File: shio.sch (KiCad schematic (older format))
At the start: 85 parts, among them J1 USB_B_Micro, U1 LM66100DCKT, U2 MAX38640AENT+, U3 NRF52840-CKAA-R7, U4 LM66100DCKT, U5 BMA400, U6 W25N01GVZEIG_TR, Y1 32.768kHz, Y2 32MHz

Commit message: All footprints are ok in layout
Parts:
- removed BAT1: 1.8V-3.6V, Shio:CR1632-THRU, symbol Device:Battery_Cell
- removed J1: USB_B_Micro, digikey-footprints:USB_Micro_B_Female_10118193-0001LF, symbol Connector:USB_B_Micro
- added J?: 10118193-0001LF, digikey-footprints:USB_Micro_B_Female_10118193-0001LF, symbol dk_USB-DVI-HDMI-Connectors:10118193-0001LF
- added U7: CR1632, Shio:CR1632-THRU, symbol CR1632:CR1632
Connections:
- wire segments 204 -> 205
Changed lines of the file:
@@
 FLASH_SCLK
-$Comp
-L Device:Battery_Cell BAT1
-U 1 1 5EF31146
-P 9650 2900
-F 0 "BAT1" H 9768 2996 50  0000 L CNN
-F 1 "1.8V-3.6V" H 9768 2905 50  0000 L CNN
-F 2 "Shio:CR1632-THRU" V 9650 2960 50  0001 C CNN
-F 3 "~" V 9650 2960 50  0001 C CNN
-	1    9650 2900
-	1    0    0    -1
-$EndComp
 $Comp
 L power:GND #PWR018
@@
 $EndComp
 $Comp
-L Connector:USB_B_Micro J1
-U 1 1 5ED1C5A9
-P 10450 2800
-F 0 "J1" H 10507 3267 50  0000 C CNN
-F 1 "USB_B_Micro" H 10507 3176 50  0000 C CNN
-F 2 "digikey-footprints:USB_Micro_B_Female_10118193-0001LF" H 10600 2750 50  0001 C CNN
-F 3 "~" H 10600 2750 50  0001 C CNN
-	1    10450 2800
-	1    0    0    -1
-$EndComp
-$Comp
 L power:GND #PWR019
 U 1 1 5ED1D7D8
-P 10450 3200
-F 0 "#PWR019" H 10450 2950 50  0001 C CNN
-F 1 "GND" H 10455 3027 50  0000 C CNN
-F 2 "" H 10450 3200 50  0001 C CNN
-F 3 "" H 10450 3200 50  0001 C CNN
-	1    10450 3200
-	1    0    0    -1
-$EndComp
-Wire Wire Line
-	10350 3200 10450 3200
-Connection ~ 10450 3200
-Wire Wire Line
-	10800 2800 10750 2800
-Wire Wire Line
-	10800 2900 10750 2900
-Text Label 10800 2800 0    50   ~ 0
+P 10900 2400
+F 0 "#PWR019" H 10900 2150 50  0001 C CNN
+F 1 "GND" H 10905 2227 50  0000 C CNN
+F 2 "" H 10900 2400 50  0001 C CNN
+F 3 "" H 10900 2400 50  0001 C CNN
+	1    10900 2400
+	1    0    0    -1
+$EndComp
+Wire Wire Line
+	10800 2400 10900 2400
+Wire Wire Line
+	10850 2100 10800 2100
+Wire Wire Line
+	10850 2200 10800 2200
+Text Label 10850 2100 0    50   ~ 0
 SWDCLK
-Text Label 10800 2900 0    50   ~ 0
+Text Label 10850 2200 0    50   ~ 0
 SWDIO
 Text Label 10650 5450 2    50   ~ 0
@@
 Connection ~ 1500 6950
 Connection ~ 1500 7250
-Wire Wire Line
-	9650 3000 9650 3050
 $Comp
 L Device:R_Small_US R10
@@
 	0    1    1    0
 $EndComp
-NoConn ~ 10750 3000
+NoConn ~ 10800 2300
 Wire Wire Line
 	8100 2950 8350 2950
-Wire Wire Line
-	9650 2700 9650 2550
 Text Label 7550 2950 0    50   ~ 0
 VDD_nRF
@@
 L power:VBUS #PWR09
 U 1 1 5F9001CA
-P 10850 2500
-F 0 "#PWR09" H 10850 2350 50  0001 C CNN
-F 1 "VBUS" H 10865 2673 50  0000 C CNN
-F 2 "" H 10850 2500 50  0001 C CNN
-F 3 "" H 10850 2500 50  0001 C CNN
-	1    10850 2500
-	1    0    0    -1
-$EndComp
-Wire Wire Line
-	10850 2500 10850 2600
-Wire Wire Line
-	10750 2600 10850 2600
+P 10900 1900
+F 0 "#PWR09" H 10900 1750 50  0001 C CNN
+F 1 "VBUS" H 10915 2073 50  0000 C CNN
+F 2 "" H 10900 1900 50  0001 C CNN
+F 3 "" H 10900 1900 50  0001 C CNN
+	1    10900 1900
+	1    0    0    -1
+$EndComp
+Wire Wire Line
+	10900 1900 10900 2000
+Wire Wire Line
+	10800 2000 10900 2000
 $Comp
 L power:+BATT #PWR010
@@
 Wire Wire Line
 	7900 1700 7950 1700
+$Comp
+L CR1632:CR1632 U7
+U 1 1 5FA2470C
+P 9750 2750
+F 0 "U7" H 9888 2719 50  0000 L CNN
+F 1 "CR1632" H 9888 2628 50  0000 L CNN
+F 2 "Shio:CR1632-THRU" H 9750 2750 50  0001 C CNN
+F 3 "" H 9750 2750 50  0001 C CNN
+	1    9750 2750
+	1    0    0    -1
+$EndComp
+Wire Wire Line
+	9650 2550 9650 2750
+Wire Wire Line
+	9650 2950 9650 3050
+$Comp
+L dk_USB-DVI-HDMI-Connectors:10118193-0001LF J?
+U 1 1 5FA5986B
+P 10500 2200
+F 0 "J?" H 10564 2945 60  0000 C CNN
+F 1 "10118193-0001LF" H 10564 2839 60  0000 C CNN
+F 2 "digikey-footprints:USB_Micro_B_Female_10118193-0001LF" H 10700 2400 60  0001 L CNN
+F 3 "http://www.amphenol-icc.com/media/wysiwyg/files/drawing/10118193.pdf" H 10700 2500 60  0001 L CNN
+F 4 "609-4616-1-ND" H 10700 2600 60  0001 L CNN "Digi-Key_PN"
+F 5 "10118193-0001LF" H 10700 2700 60  0001 L CNN "MPN"
+F 6 "Connectors, Interconnects" H 10700 2800 60  0001 L CNN "Category"
+F 7 "USB, DVI, HDMI Connectors" H 10700 2900 60  0001 L CNN "Family"
+F 8 "http://www.amphenol-icc.com/media/wysiwyg/files/drawing/10118193.pdf" H 10700 3000 60  0001 L CNN "DK_Datasheet_Link"
+F 9 "/product-detail/en/amphenol-icc-fci/10118193-0001LF/609-4616-1-ND/2785380" H 10700 3100 60  0001 L CNN "DK_Detail_Page"
+F 10 "CONN RCPT USB2.0 MICRO B SMD R/A" H 10700 3200 60  0001 L CNN "Description"
+F 11 "Amphenol ICC (FCI)" H 10700 3300 60  0001 L CNN "Manufacturer"
+F 12 "Active" H 10700 3400 60  0001 L CNN "Status"
+	1    10500 2200
+	1    0    0    -1
+$EndComp
+$Comp
+L power:GND #PWR?
+U 1 1 5FA8A219
+P 10400 2850
+F 0 "#PWR?" H 10400 2600 50  0001 C CNN
+F 1 "GND" H 10405 2677 50  0000 C CNN
+F 2 "" H 10400 2850 50  0001 C CNN
+F 3 "" H 10400 2850 50  0001 C CNN
+	1    10400 2850
+	1    0    0    -1
+$EndComp
+Wire Wire Line
+	10400 2800 10400 2850
 $EndSCHEMATC

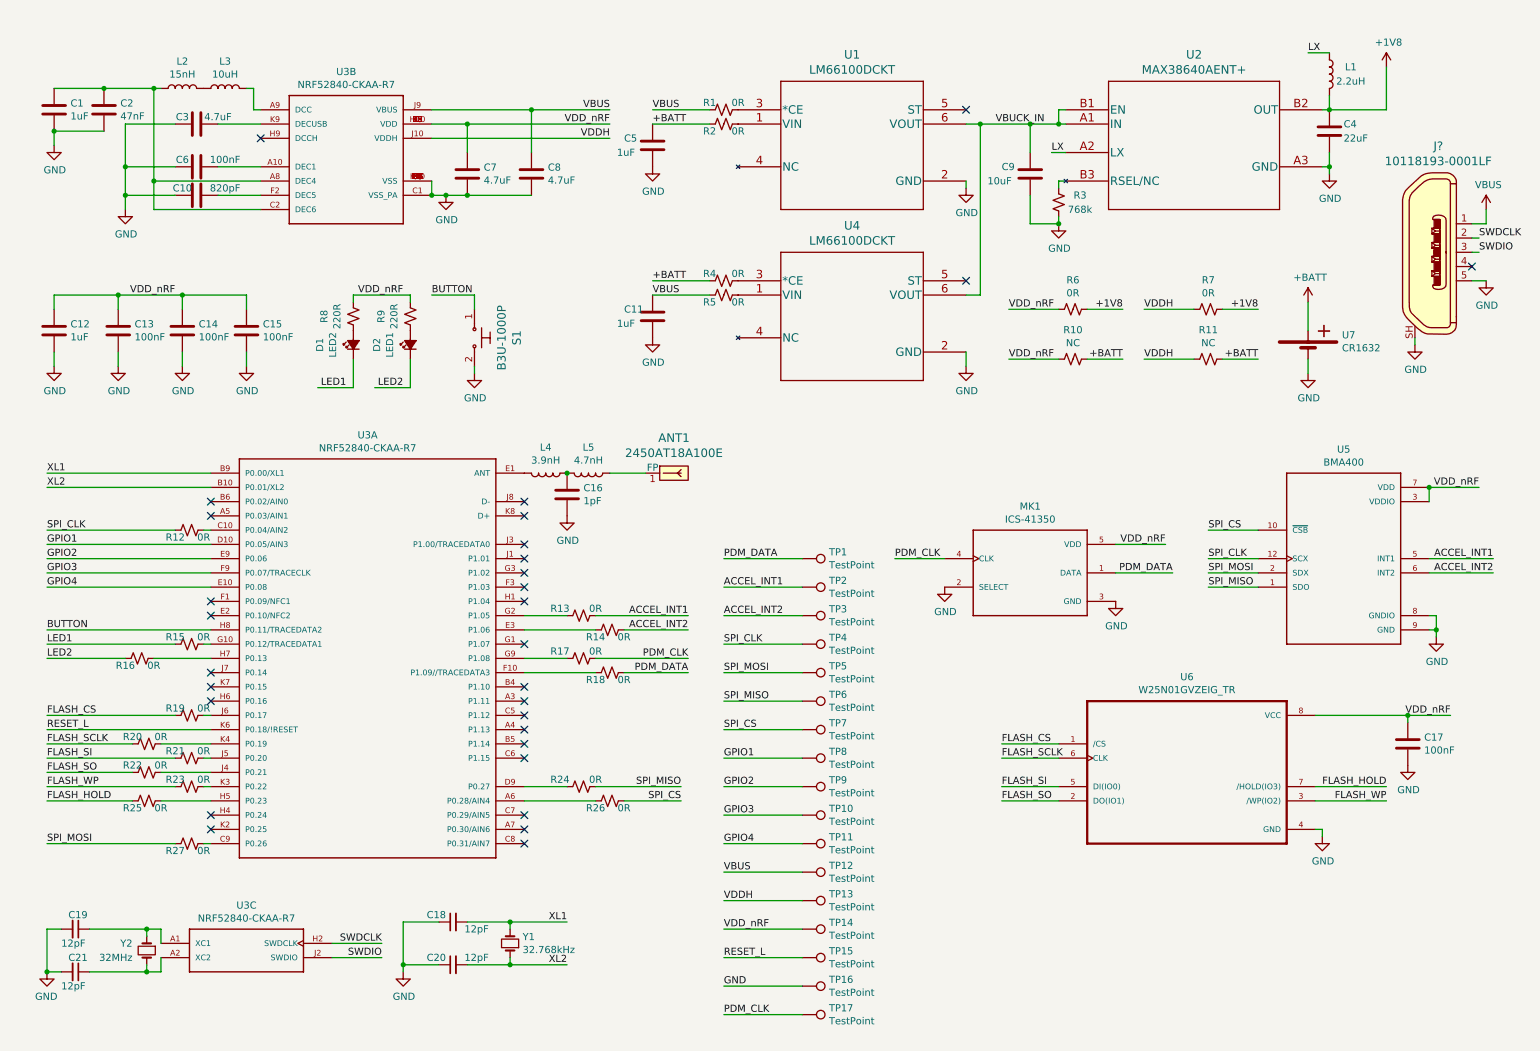
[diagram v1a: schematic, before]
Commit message: nRF52 reference placement done
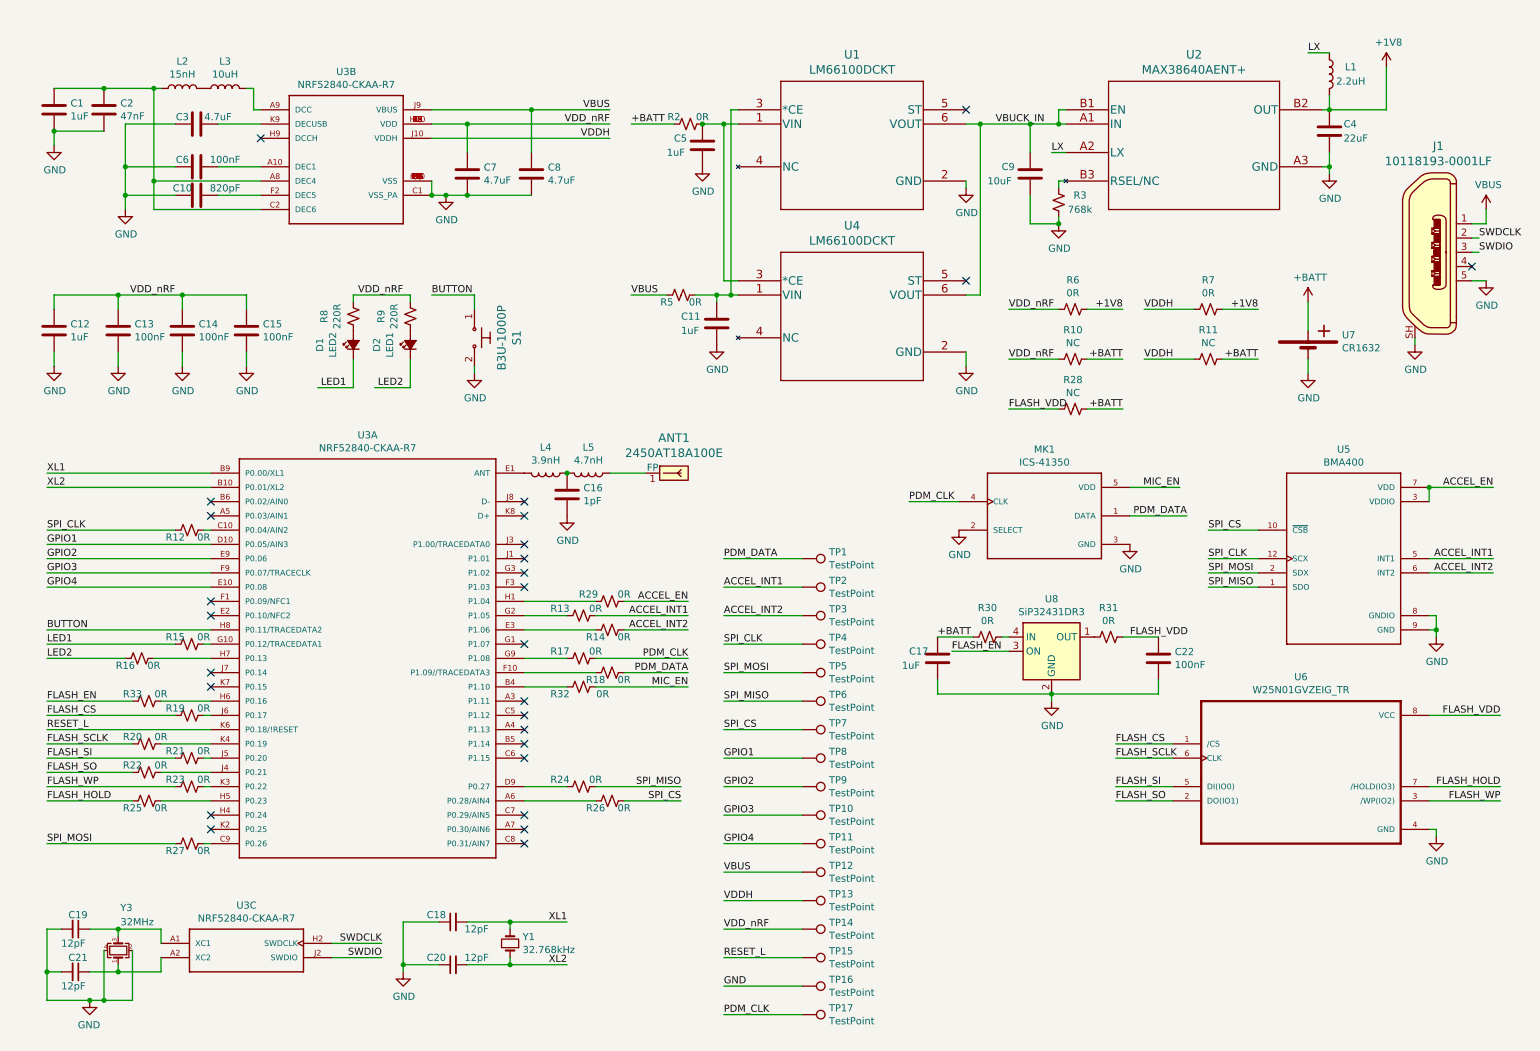
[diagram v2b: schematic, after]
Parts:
- removed R1, R4: 0R, Resistor_SMD:R_0201_0603Metric, symbol Device:R_Small_US
- removed Y2: 32MHz, Crystal:Crystal_SMD_2016-4Pin_2.0x1.6mm, symbol Device:Crystal_Small
- added C22: 100nF, Capacitor_SMD:C_0201_0603Metric, symbol Device:C
- added R28: NC, Resistor_SMD:R_0402_1005Metric, symbol Device:R_Small_US
- added R29, R32, R33: 0R, Resistor_SMD:R_0201_0603Metric, symbol Device:R_Small_US
- added R30, R31: 0R, Resistor_SMD:R_0402_1005Metric, symbol Device:R_Small_US
- added U8: SiP32431DR3, Package_TO_SOT_SMD:SOT-363_SC-70-6, symbol Power_Management:SiP32431DR3
- added Y3: 32MHz, Crystal:Crystal_SMD_2016-4Pin_2.0x1.6mm, symbol Device:Crystal_GND24_Small
- C17: value 100nF -> 1uF; footprint Capacitor_SMD:C_0201_0603Metric -> Capacitor_SMD:C_0402_1005Metric
- gave numbers to parts that had none: 1
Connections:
- net +BATT: now also C17.1, R28.1, R30.2; no longer C5.1
- net GND: now also C22.2, U8.2 (GND), U8.5 (GND), Y3.2, Y3.4
- net VBUS: no longer C11.1
- net VDD_nRF: no longer C17.1, MK1.5 (VDD), U5.3 (VDDIO), U5.7 (VDD), U6.8 (VCC)
- net at C19.1, U3.A1 (XC1): now also Y3.3
- net at C21.1, U3.A2 (XC2): now also Y3.1
- net at U3.B4 (P1.10): now also R32.2
- net at U3.H1 (P1.04): now also R29.2
- net at U3.H6 (P0.16): now also R33.1
- net at R2.1, U1.1 (VIN): now also C5.1, U4.3 (*CE)
- net at U1.3 (*CE): now also C11.1, R5.1, U4.1 (VIN)
- new net: R31.2, U8.1 (OUT)
- new net: R30.1, U8.4 (IN)
- new net ACCEL_EN: R29.1, U5.3 (VDDIO), U5.7 (VDD)
- new net FLASH_EN: R33.2, U8.3 (ON)
- new net FLASH_VDD: C22.1, R28.2, R31.1, U6.8 (VCC)
- new net MIC_EN: MK1.5 (VDD), R32.1
- no-connect marks 30 -> 27
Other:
- moved on the sheet: C11, C5, MK1, R2, R5, U6

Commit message: First pass at placement complete
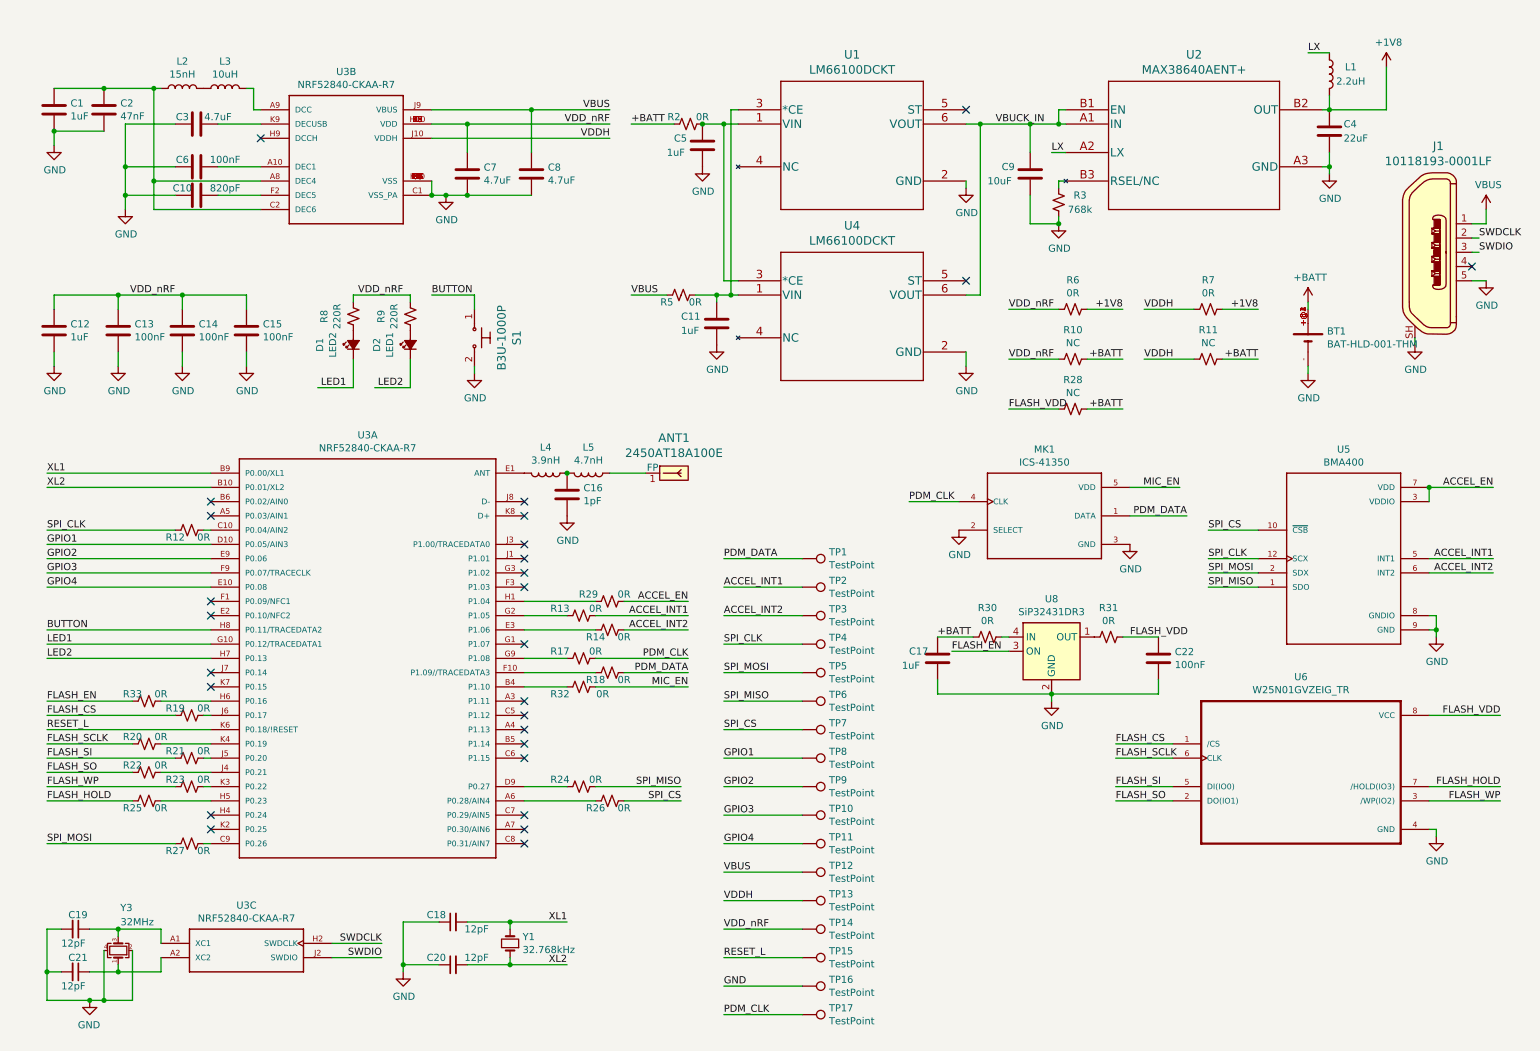
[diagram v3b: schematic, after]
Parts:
- removed R15, R16: 0R, Resistor_SMD:R_0201_0603Metric, symbol Device:R_Small_US
- removed U7: CR1632, Shio:CR1632-THRU, symbol CR1632:CR1632
- added BT1: BAT-HLD-001-THM, maruchi-kicad-library:LINX_BAT-HLD-001-THM, symbol BAT-HLD-001-THM:BAT-HLD-001-THM
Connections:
- net +BATT: now also BT1.+@1 (+), BT1.+@2 (+), BT1.+@3 (+), BT1.+@4 (+)
- net GND: now also BT1.-
- net LED1: now also U3.G10 (P0.12/TRACEDATA1)
- net LED2: now also U3.H7 (P0.13)

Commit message: Started layout
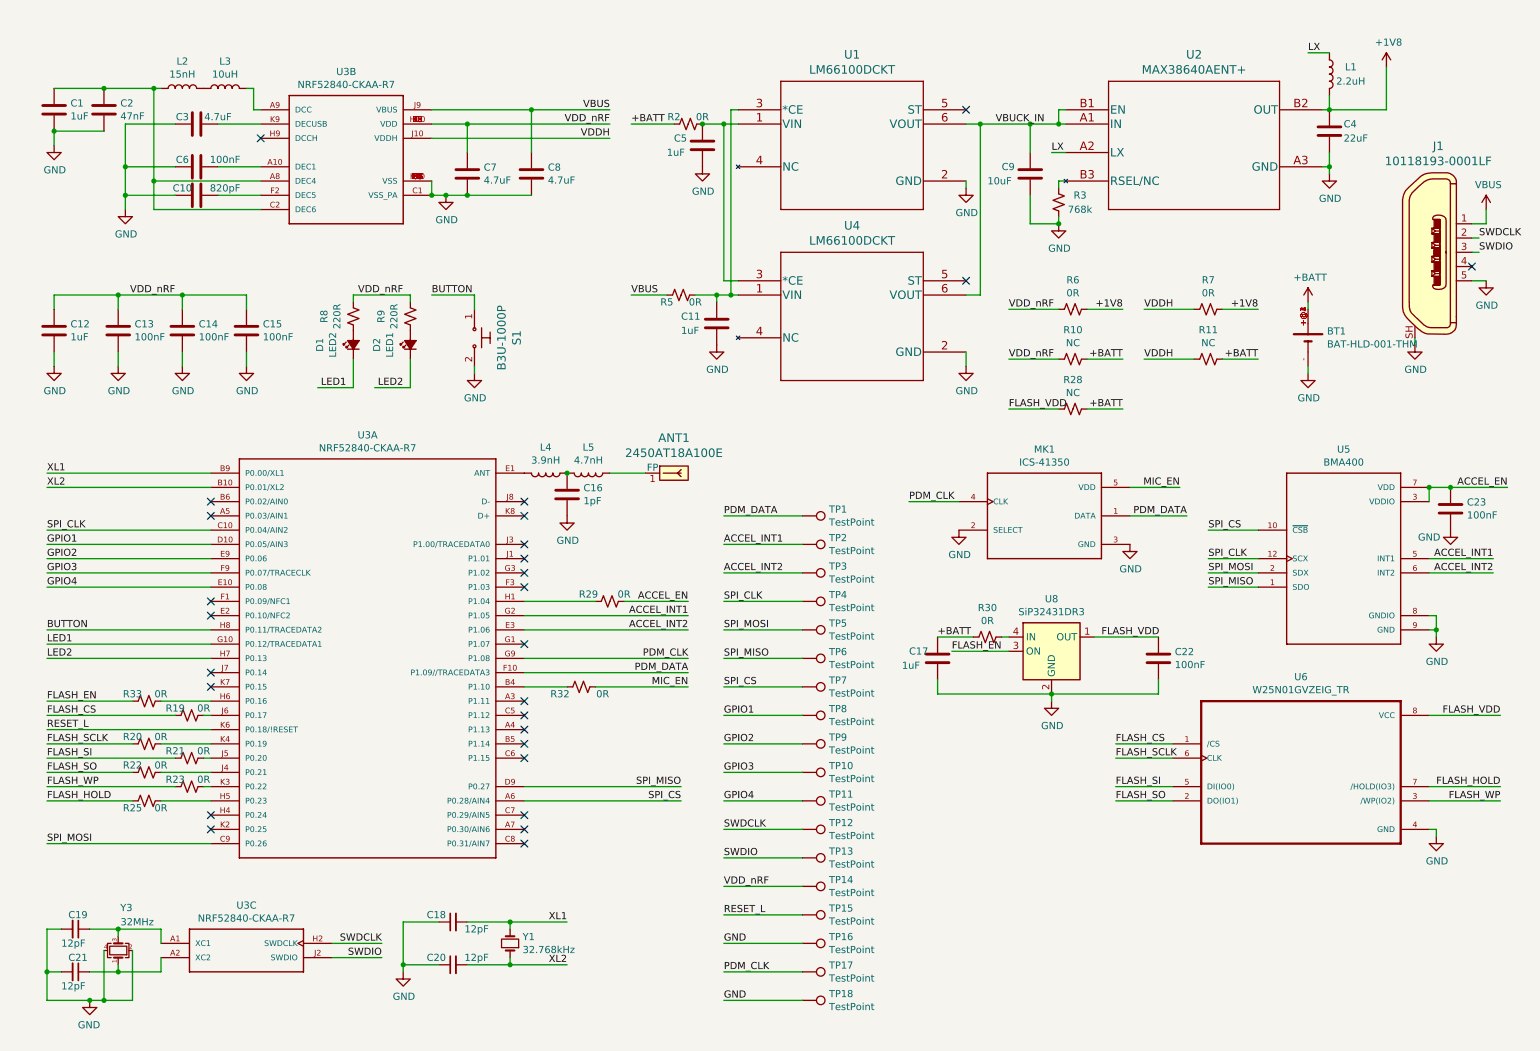
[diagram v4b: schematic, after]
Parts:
- removed R12, R13, R14, R17, R18, R24, R26, R27: 0R, Resistor_SMD:R_0201_0603Metric, symbol Device:R_Small_US
- removed R31: 0R, Resistor_SMD:R_0402_1005Metric, symbol Device:R_Small_US
- added C23: 100nF, Capacitor_SMD:C_0201_0603Metric, symbol Device:C
- added TP18: TestPoint, TestPoint:TestPoint_Pad_D0.5mm, symbol Connector:TestPoint
- TP1, TP10, TP11, TP12, TP13, TP14, TP15, TP16, TP17, TP2, TP3, TP4, TP5, TP6, TP7, TP8, TP9: footprint TestPoint:TestPoint_Pad_D1.0mm -> TestPoint:TestPoint_Pad_D0.5mm
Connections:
- net ACCEL_EN: now also C23.1
- net ACCEL_INT1: now also U3.G2 (P1.05)
- net ACCEL_INT2: now also U3.E3 (P1.06)
- net FLASH_VDD: now also U8.1 (OUT)
- net GND: now also C23.2, TP18.1
- net PDM_CLK: now also U3.G9 (P1.08)
- net PDM_DATA: now also U3.F10 (P1.09//TRACEDATA3)
- net SPI_CLK: now also U3.C10 (P0.04/AIN2)
- net SPI_CS: now also U3.A6 (P0.28/AIN4)
- net SPI_MISO: now also U3.D9 (P0.27)
- net SPI_MOSI: now also U3.C9 (P0.26)
- net SWDCLK: now also TP12.1
- net SWDIO: now also TP13.1
- net VBUS: no longer TP12.1
- net VDDH: no longer TP13.1
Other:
- moved on the sheet: TP1, TP10, TP11, TP14, TP15, TP16, TP17, TP2, TP3, TP4, TP5, TP6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
